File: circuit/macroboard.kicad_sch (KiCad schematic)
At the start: 29 parts, among them SW1 CherryMX, SW10 CherryMX, SW11 CherryMX, SW12 CherryMX, SW13 SW_Push, SW14 SW_DIP_x01, SW2 CherryMX, SW3 CherryMX, SW4 CherryMX, SW5 CherryMX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

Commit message: add basic pcb layout (no routing)
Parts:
- added H1, H2, H3, H4, H5, H6: MountingHole, MountingHole:MountingHole_2.1mm, symbol Mechanical:MountingHole
- U1: footprint Package_QFP:TQFP-44_10x10mm_P0.8mm -> MCUs:Arduino Pro Micro

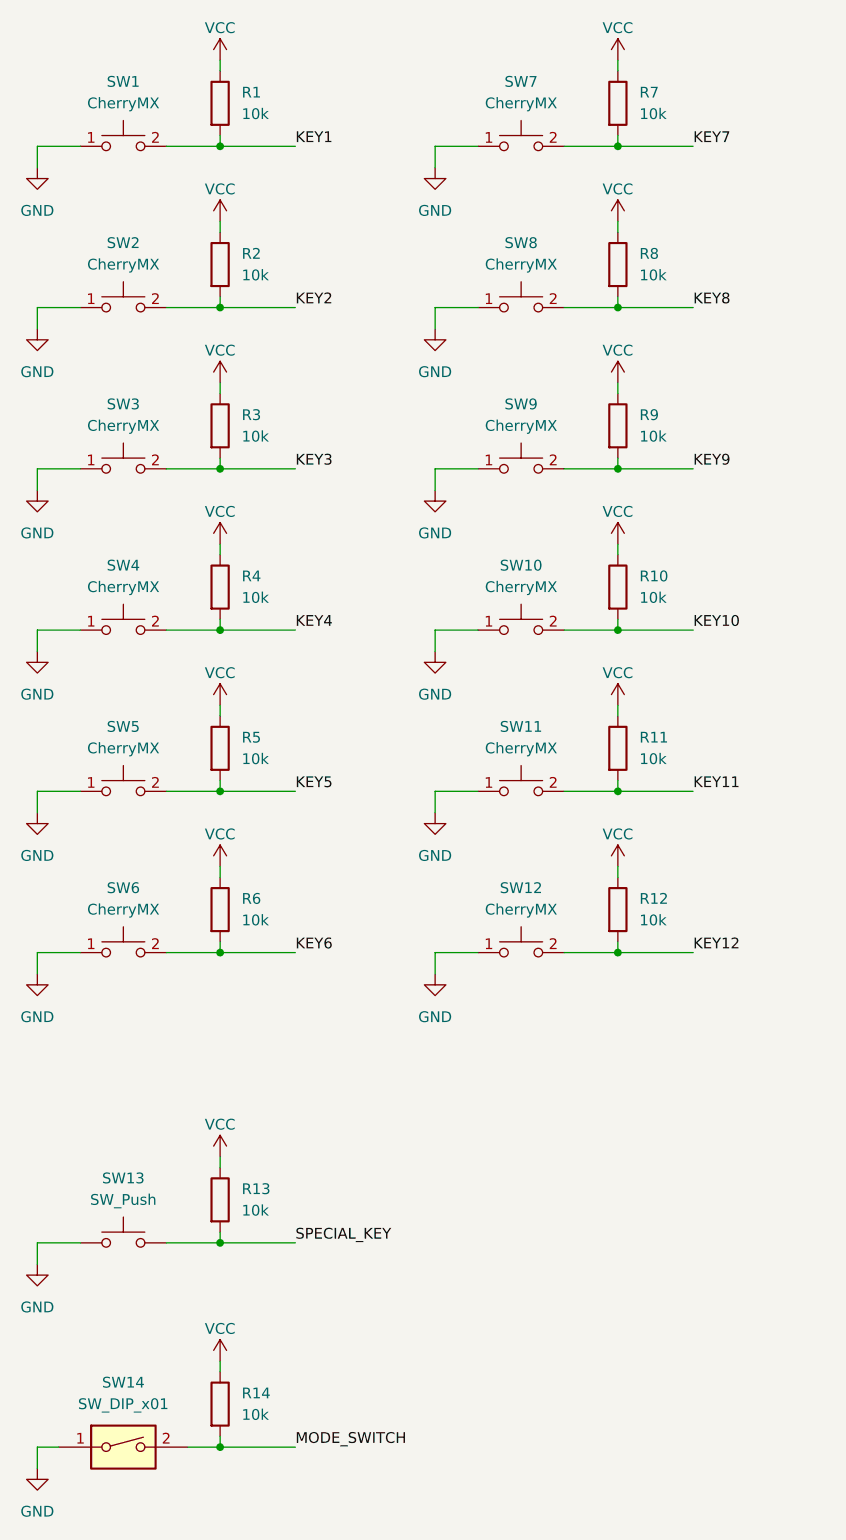
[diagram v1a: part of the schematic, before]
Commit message: add reusable debounce circuit with solder jumper
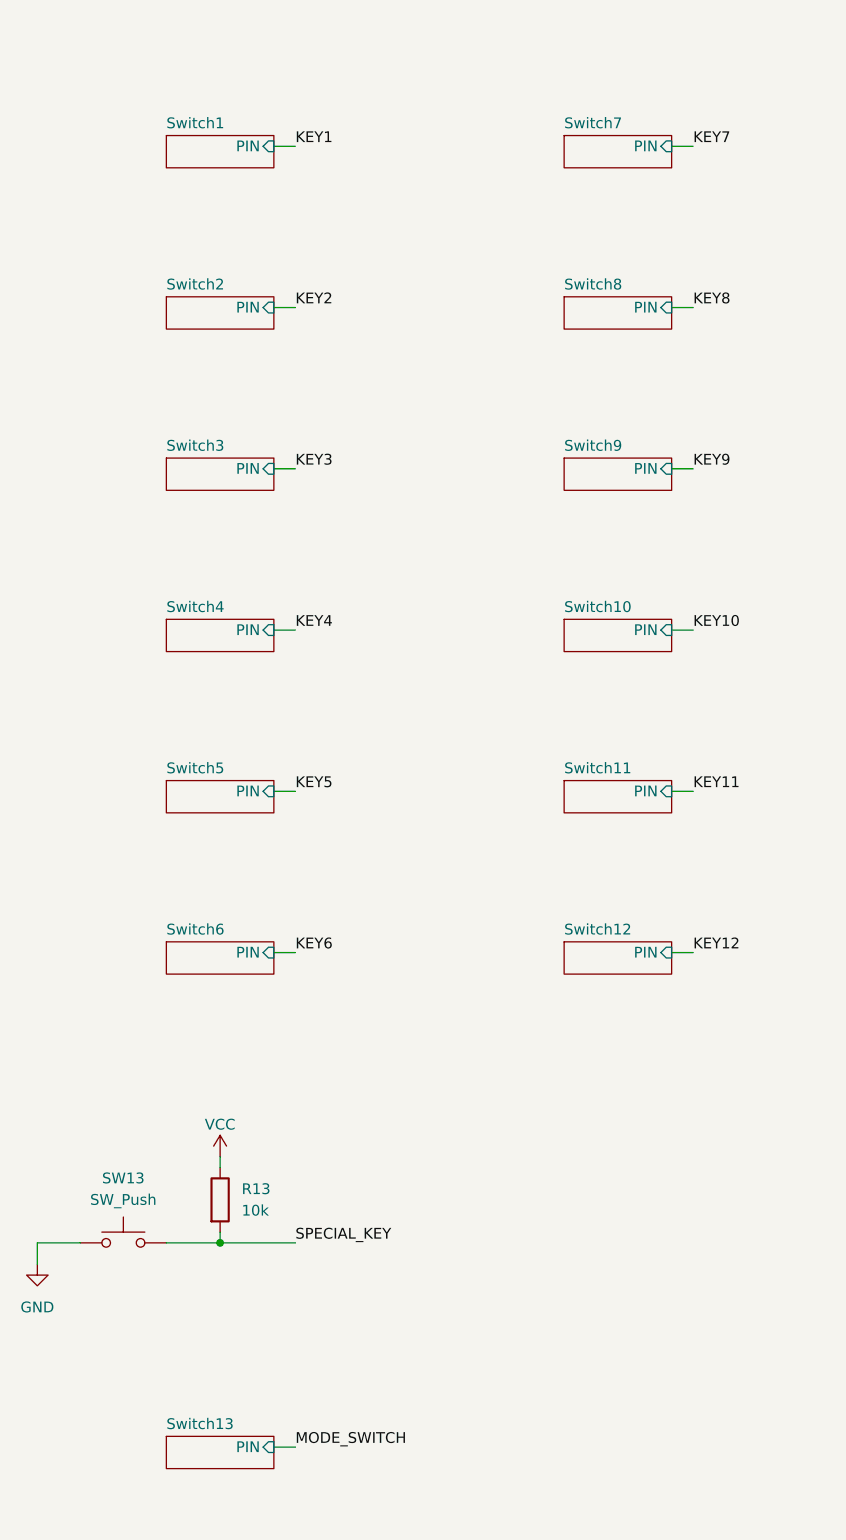
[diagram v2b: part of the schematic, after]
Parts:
- removed R1, R10, R11, R12, R14, R2, R3, R4, R5, R6, R7, R8, R9: 10k, Resistor_SMD:R_0805_2012Metric, symbol Device:R
- removed SW1, SW10, SW11, SW12, SW2, SW3, SW4, SW5, SW6, SW7, SW8, SW9: CherryMX, CherryMX_KailhSocket:CherryMX_1.00u_KailhSocket, symbol CherryMX:CherryMX
- removed SW14: SW_DIP_x01, symbol Switch:SW_DIP_x01
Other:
- added sheet Switch1 (switch.kicad_sch)
- added sheet Switch10 (switch.kicad_sch)
- added sheet Switch11 (switch.kicad_sch)
- added sheet Switch12 (switch.kicad_sch)
- added sheet Switch13 (switch.kicad_sch)
- added sheet Switch2 (switch.kicad_sch)
- added sheet Switch3 (switch.kicad_sch)
- added sheet Switch4 (switch.kicad_sch)
- added sheet Switch5 (switch.kicad_sch)
- added sheet Switch6 (switch.kicad_sch)
- added sheet Switch7 (switch.kicad_sch)
- added sheet Switch8 (switch.kicad_sch)
- added sheet Switch9 (switch.kicad_sch)

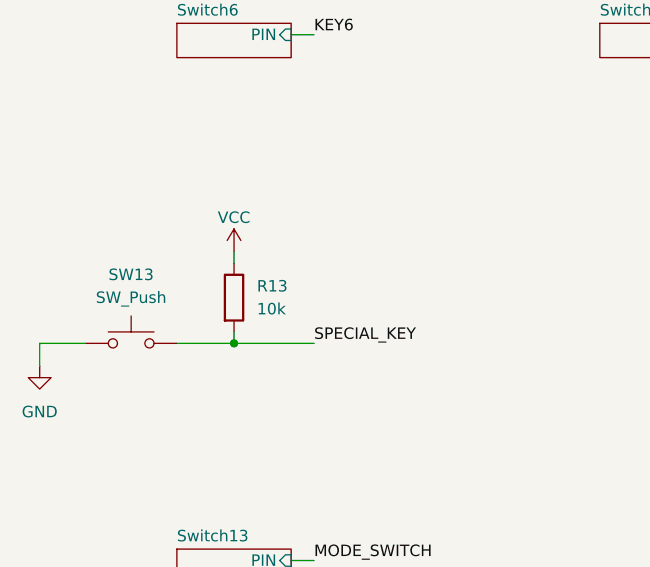
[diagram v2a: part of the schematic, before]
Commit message: add custom footprints, improve layout
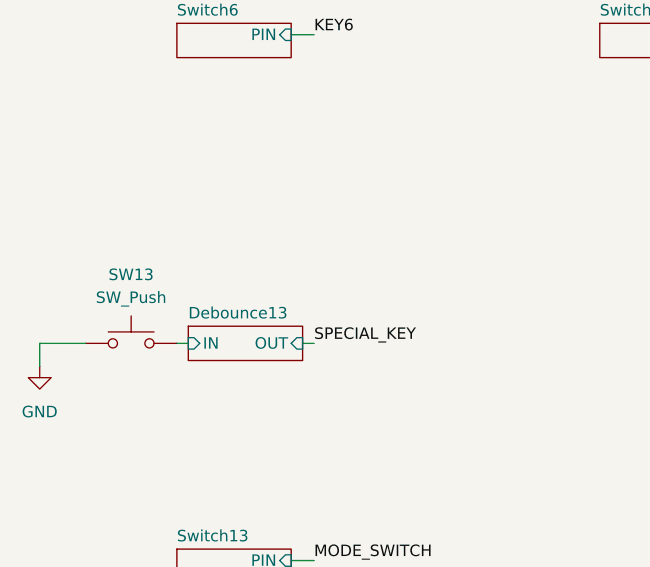
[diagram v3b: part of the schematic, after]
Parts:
- removed R13: 10k, Resistor_SMD:R_0805_2012Metric, symbol Device:R
- SW13: footprint (none) -> custom:AUX Jack 6.3mm External
- U1: footprint MCUs:Arduino Pro Micro -> custom:Arduino Pro Micro
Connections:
- net SPECIAL_KEY: no longer SW13.2
- new net Debounce13/IN: SW13.2
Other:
- added sheet Debounce13 (switch_debounce.kicad_sch)
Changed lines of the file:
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@@
-	)
-	(junction
-		(at 57.15 161.29)
-		(diameter 0)
-		(color 0 0 0 0)
 	)
 	(junction
@@
 	(wire
 		(pts
+			(xy 64.77 161.29) (xy 66.04 161.29)
+		)
+		(stroke
+			(width 0)
+			(type default)
+		)
+	)
+	(wire
+		(pts
 			(xy 63.5 107.95) (xy 66.04 107.95)
 		)
@@
 	(wire
 		(pts
-			(xy 57.15 161.29) (xy 66.04 161.29)
-		)
-		(stroke
-			(width 0)
-			(type default)
-		)
-	)
-	(wire
-		(pts
 			(xy 233.68 69.85) (xy 231.14 69.85)
 		)
@@
 	(wire
 		(pts
+			(xy 50.8 161.29) (xy 52.07 161.29)
+		)
+		(stroke
+			(width 0)
+			(type default)
+		)
+	)
+	(wire
+		(pts
 			(xy 110.49 88.9) (xy 113.03 88.9)
 		)
@@
 	(wire
 		(pts
-			(xy 57.15 152.4) (xy 57.15 151.13)
-		)
-		(stroke
-			(width 0)
-			(type default)
-		)
-	)
-	(wire
-		(pts
-			(xy 57.15 160.02) (xy 57.15 161.29)
-		)
-		(stroke
-			(width 0)
-			(type default)
-		)
-	)
-	(wire
-		(pts
 			(xy 213.36 123.19) (xy 213.36 124.46)
-		)
-		(stroke
-			(width 0)
-			(type default)
-		)
-	)
-	(wire
-		(pts
-			(xy 50.8 161.29) (xy 57.15 161.29)
 		)
 		(stroke
@@
 	)
 	(symbol
-		(lib_id "Device:R")
-		(at 57.15 156.21 0)
-		(unit 1)
-		(exclude_from_sim no)
-		(in_bom yes)
-		(on_board yes)
-		(dnp no)
-		(fields_autoplaced yes)
-		(property "Reference" "R13"
-			(at 59.69 154.9399 0)
-			(effects
-				(font
-					(size 1.27 1.27)
-				)
-				(justify left)
-			)
-		)
-		(property "Value" "10k"
-			(at 59.69 157.4799 0)
-			(effects
-				(font
-					(size 1.27 1.27)
-				)
-				(justify left)
-			)
-		)
-		(property "Footprint" "Resistor_SMD:R_0805_2012Metric"
-			(at 55.372 156.21 90)
-			(effects
-				(font
-					(size 1.27 1.27)
-				)
-				(hide yes)
-			)
-		)
-		(property "Datasheet" "~"
-			(at 57.15 156.21 0)
-			(effects
-				(font
-					(size 1.27 1.27)
-				)
-				(hide yes)
-			)
-		)
-		(property "Description" "Resistor"
-			(at 57.15 156.21 0)
-			(effects
-				(font
-					(size 1.27 1.27)
-				)
-				(hide yes)
-			)
-		)
-		(pin "1"
-		)
-		(pin "2"
-		)
-		(instances
-			(project "macroboard"
-				(path "/eb2ff33f-8c2d-40be-bc06-8483c3a89847"
-					(reference "R13")
-					(unit 1)
-				)
-			)
-		)
-	)
-	(symbol
-		(lib_id "power:VCC")
-		(at 57.15 151.13 0)
-		(unit 1)
-		(exclude_from_sim no)
-		(in_bom yes)
-		(on_board yes)
-		(dnp no)
-		(property "Reference" "#PWR025"
-			(at 57.15 154.94 0)
-			(effects
-				(font
-					(size 1.27 1.27)
-				)
-				(hide yes)
-			)
-		)
-		(property "Value" "VCC"
-			(at 57.15 147.32 0)
-			(effects
-				(font
-					(size 1.27 1.27)
-				)
-			)
-		)
-		(property "Footprint" ""
-			(at 57.15 151.13 0)
-			(effects
-				(font
-					(size 1.27 1.27)
-				)
-				(hide yes)
-			)
-		)
-		(property "Datasheet" ""
-			(at 57.15 151.13 0)
-			(effects
-				(font
-					(size 1.27 1.27)
-				)
-				(hide yes)
-			)
-		)
-		(property "Description" "Power symbol creates a global label with name \"VCC\""
-			(at 57.15 151.13 0)
-			(effects
-				(font
-					(size 1.27 1.27)
-				)
-				(hide yes)
-			)
-		)
-		(pin "1"
-		)
-		(instances
-			(project "macroboard"
-				(path "/eb2ff33f-8c2d-40be-bc06-8483c3a89847"
-					(reference "#PWR025")
-					(unit 1)
-				)
-			)
-		)
-	)
-	(symbol
 		(lib_id "MCU_Microchip_ATmega:ATmega32U4-A")
 		(at 215.9 77.47 0)
@@
 			)
 		)
-		(property "Footprint" "MCUs:Arduino Pro Micro"
+		(property "Footprint" "custom:Arduino Pro Micro"
 			(at 215.9 77.47 0)
 			(effects
@@
 			)
 		)
-		(property "Footprint" ""
+		(property "Footprint" "custom:AUX Jack 6.3mm External"
 			(at 45.72 156.21 0)
 			(effects
@@
 				)
 			)
+		)
+	)
+	(sheet
+		(at 52.07 159.385)
+		(size 12.7 3.81)
+		(exclude_from_sim no)
+		(in_bom yes)
+		(on_board yes)
+		(dnp no)
+		(fields_autoplaced yes)
+		(stroke
+			(width 0.1524)
+			(type solid)
+		)
+		(fill
+			(color 0 0 0 0.0000)
+		)
+		(property "Sheetname" "Debounce13"
+			(at 52.07 158.6734 0)
+			(effects
+				(font
+					(size 1.27 1.27)
+				)
+				(justify left bottom)
+			)
+		)
+		(property "Sheetfile" "switch_debounce.kicad_sch"
+			(at 52.07 163.7796 0)
+			(effects
+				(font
+					(size 1.27 1.27)
+				)
+				(justify left top)
+				(hide yes)
+			)
+		)
+		(pin "IN" input
+			(at 52.07 161.29 180)
+			(effects
+				(font
+					(size 1.27 1.27)
+				)
+				(justify left)
+			)
+		)
+		(pin "OUT" input
+			(at 64.77 161.29 0)
+			(effects
+				(font
+					(size 1.27 1.27)
+				)
+				(justify right)
+			)
+		)
+		(instances
+			(project "macroboard"
+				(path "/eb2ff33f-8c2d-40be-bc06-8483c3a89847"
+					(page "28")
+				)
+			)

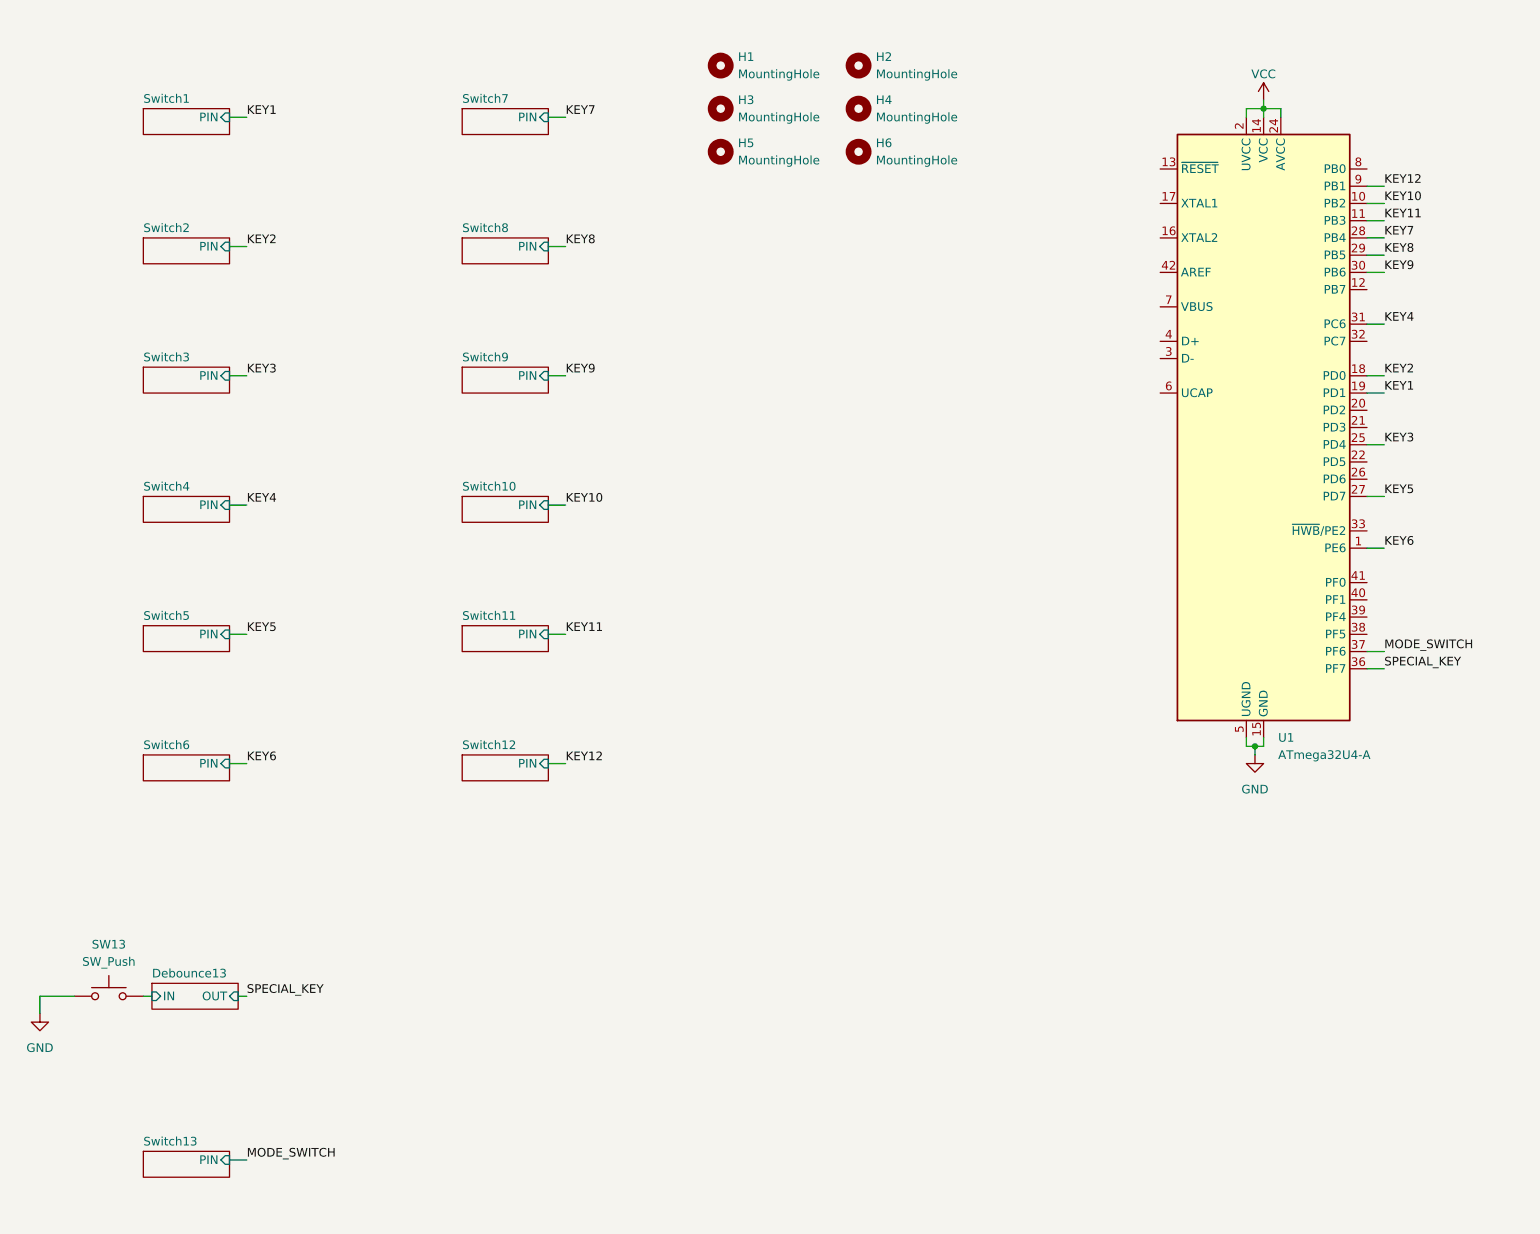
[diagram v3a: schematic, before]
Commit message: add special switches, add routing
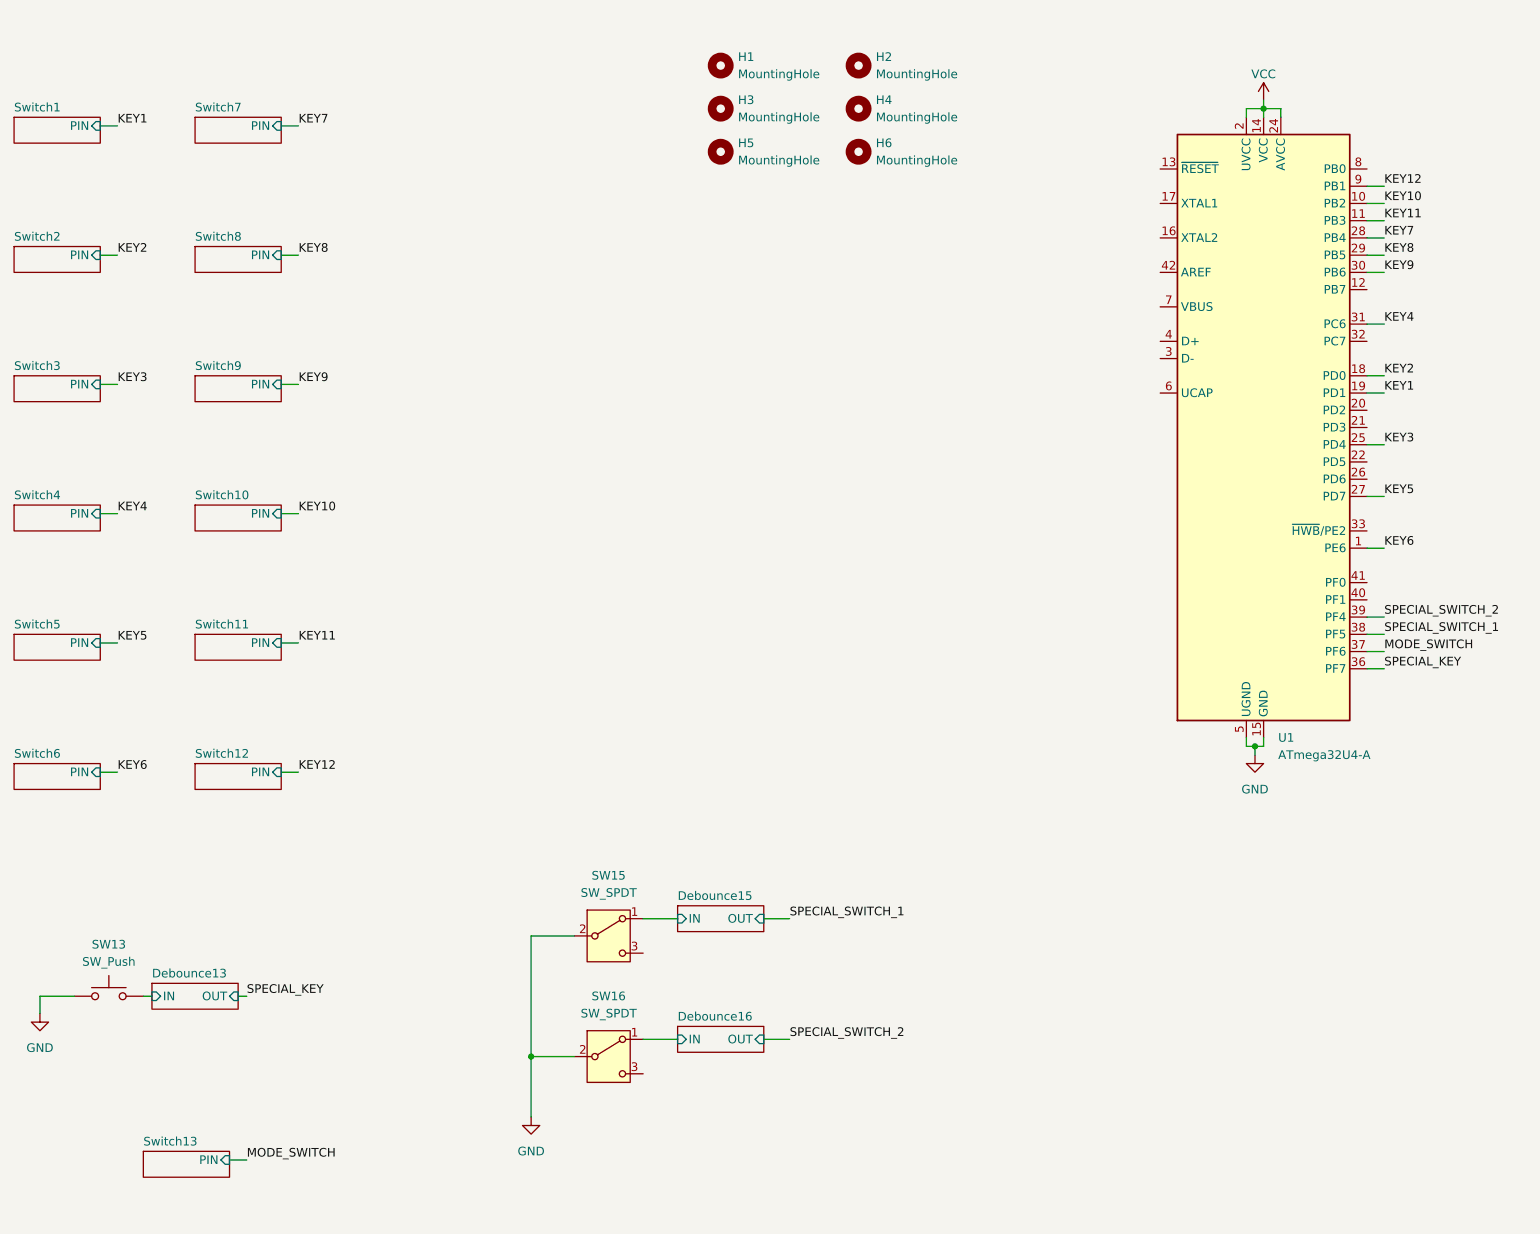
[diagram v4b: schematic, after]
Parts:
- added SW15, SW16: SW_SPDT, Button_Switch_THT:SW_Slide_SPDT_Angled_CK_OS102011MA1Q, symbol Switch:SW_SPDT
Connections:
- net GND: now also SW15.2 (B), SW16.2 (B)
- net SPECIAL_SWITCH_1: now reaches U1.38 (PF5)
- net SPECIAL_SWITCH_2: now reaches U1.39 (PF4)
- new net Debounce15/IN: SW15.1 (A)
- new net Debounce16/IN: SW16.1 (A)
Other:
- added sheet Debounce15 (switch_debounce.kicad_sch)
- added sheet Debounce16 (switch_debounce.kicad_sch)
